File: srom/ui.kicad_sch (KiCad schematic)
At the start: 17 parts, among them J301 Conn_01x10_Female, J303 Conn_01x03_Female, SW301 SW_MEC_5E, SW302 RotaryEncoder_Switch, SW303 SW_MEC_5E, U301 Pico-3 UI

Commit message: first draft of daughterboard taking shape
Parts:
- removed D301, D302, D303, D304, D305, D306, D307, D308: LED_Small, LED_THT:LED_D3.0mm, symbol Device:LED_Small
- removed SW301, SW303: SW_MEC_5E, Button_Switch_THT:SW_PUSH_6mm_H4.3mm, symbol Switch:SW_MEC_5E
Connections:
- net 3V3_PICO3: now also J?.2 (Pin_2); no longer J?.5 (Pin_5)
- net ACTION_SW: now also J?.5 (Pin_5); no longer J?.2 (Pin_2)
- net CANCEL_SW: now also J?.6 (Pin_6); no longer J?.1 (Pin_1)
- net GND: now also J?.1 (Pin_1); no longer J?.6 (Pin_6)
- net OLED_SCK: now also J?.3 (Pin_3); no longer J?.4 (Pin_4)
- net OLED_SDA: now also J?.4 (Pin_4); no longer J?.3 (Pin_3)
- no-connect marks 16 -> 8
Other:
- note added: "Connection off to the 8 motor LEDs. The LEDs themselves are mounted on the daugherboard."
- note added: "I2C connection to OLED screen. Internal pullups work fine. SSH1106 based 1.3" screen is ideal, but C SDK doesn't seem to support it. Use SSH1306 0.96" screen for now, that's supported. The external user interface devices board connects here and on the connector for the LEDs. These provide a decent physical connection for the daughterboard."
- note removed: "I2C connection to OLED screen. Internal pullups work fine. SSH1106 based 1.3" screen is ideal, but C SDK doesn't seem to support it. Use SSH1306 0.96" screen for now, that's supported."
- note removed: "LED are excluded from the board. The signals from the GPIOs go to a header, LEDs connect to the header and are physically mounted on a panel."
- note removed: "LEDs for microdrive motor on. Use 3mm red one, like on the original drive. MOVE THESE TO EXTERNAL BOARD"
- note removed: "Two active-low switched inputs to the Pico UI. "Action" and "Cancel" UI functions. MOVE THESE TO EXTERNAL BOARD"
- moved on the sheet: J301, J?, R308

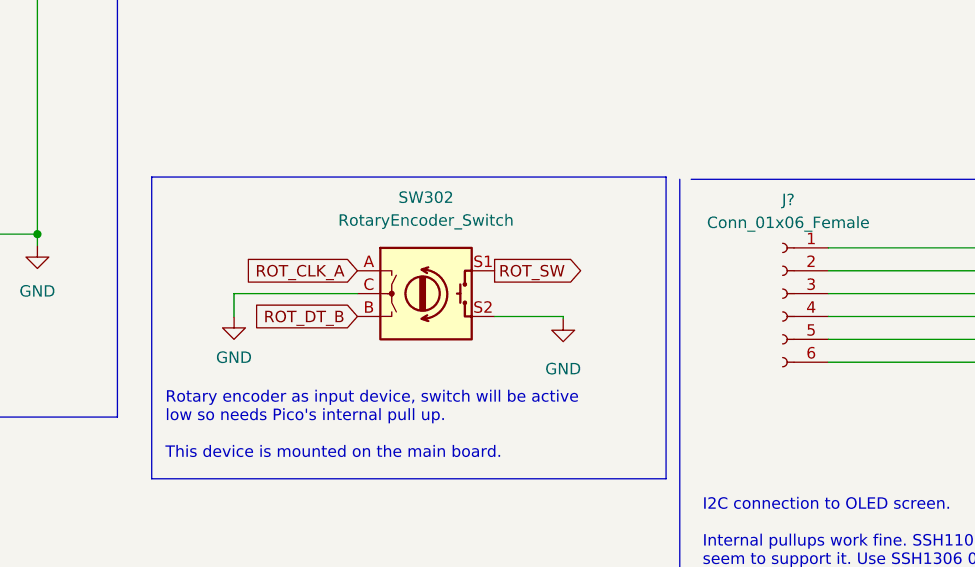
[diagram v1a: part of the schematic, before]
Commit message: board layout work, 4 layers
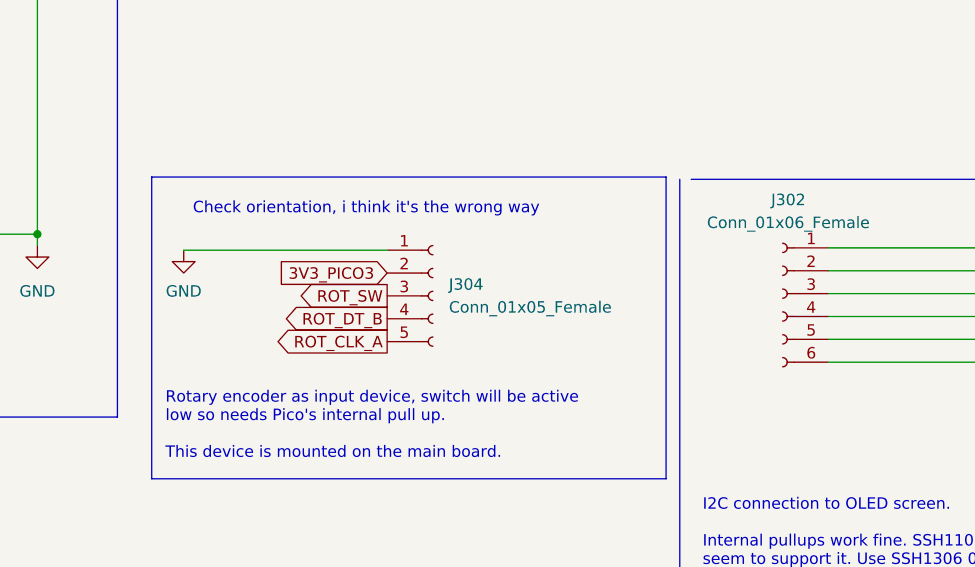
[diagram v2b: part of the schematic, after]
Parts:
- removed SW302: RotaryEncoder_Switch, Rotary_Encoder:RotaryEncoder_Bourns_Vertical_PEC12R-3xxxF-Sxxxx, symbol Device:RotaryEncoder_Switch
- added J304: Conn_01x05_Female, Connector_PinHeader_2.54mm:PinHeader_1x05_P2.54mm_Vertical, symbol Connector:Conn_01x05_Female
- J301: footprint (none) -> Connector_PinHeader_2.54mm:PinHeader_1x10_P2.54mm_Vertical
- J302: renamed from J?; footprint (none) -> Connector_PinHeader_2.54mm:PinHeader_1x06_P2.54mm_Vertical
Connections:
- net 3V3_PICO3: now also J304.2 (Pin_2)
- net GND: now also J304.1 (Pin_1)
- net ROT_CLK_A: now also J304.5 (Pin_5)
- net ROT_DT_B: now also J304.4 (Pin_4)
- net ROT_SW: now also J304.3 (Pin_3)
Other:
- note added: "Check orientation, i think it's the wrong way"
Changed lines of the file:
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@@
     (stroke (width 0) (type default) (color 0 0 0 0))
   )
-  (wire (pts (xy 141.224 118.364) (xy 141.224 120.904))
-    (stroke (width 0) (type default) (color 0 0 0 0))
-  )
-  (wire (pts (xy 141.224 118.364) (xy 154.94 118.364))
+  (wire (pts (xy 135.636 113.538) (xy 158.242 113.538))
     (stroke (width 0) (type default) (color 0 0 0 0))
   )
@@
     (stroke (width 0) (type default) (color 0 0 0 0))
   )
-  (wire (pts (xy 170.18 120.904) (xy 177.8 120.904))
-    (stroke (width 0) (type default) (color 0 0 0 0))
-  )
   (wire (pts (xy 60.96 167.132) (xy 59.182 167.132))
     (stroke (width 0) (type default) (color 0 0 0 0))
@@
   )
   (wire (pts (xy 90.17 40.64) (xy 119.38 40.64))
-    (stroke (width 0) (type default) (color 0 0 0 0))
-  )
-  (wire (pts (xy 177.8 120.904) (xy 177.8 121.158))
     (stroke (width 0) (type default) (color 0 0 0 0))
   )
@@
     (effects (font (size 1.27 1.27)) (justify left bottom))
   )
+  (text "Check orientation, i think it's the wrong way\n" (at 136.652 109.728 0)
+    (effects (font (size 1.27 1.27)) (justify left bottom))
+  )
   (text "GPIOs for the\nrotary encoder.\nDon't need SW." (at 26.924 60.96 0)
     (effects (font (size 1.27 1.27)) (justify left bottom))
@@
     )
   )
-  (global_label "ROT_CLK_A" (shape input) (at 154.94 115.824 180) (fields_autoplaced)
-    (effects (font (size 1.27 1.27)) (justify right))
-    (property "Intersheet References" "${INTERSHEET_REFS}" (id 0) (at 142.3669 115.7446 0)
+  (global_label "ROT_CLK_A" (shape output) (at 158.242 123.698 180) (fields_autoplaced)
+    (effects (font (size 1.27 1.27)) (justify right))
+    (property "Intersheet References" "${INTERSHEET_REFS}" (id 0) (at 145.6689 123.6186 0)
       (effects (font (size 1.27 1.27)) (justify right) hide)
     )
@@
     )
   )
+  (global_label "3V3_PICO3" (shape input) (at 158.242 116.078 180) (fields_autoplaced)
+    (effects (font (size 1.27 1.27)) (justify right))
+    (property "Intersheet References" "${INTERSHEET_REFS}" (id 0) (at 145.6689 115.9986 0)
+      (effects (font (size 1.27 1.27)) (justify right) hide)
+    )
+  )
   (global_label "OLED_SDA" (shape output) (at 54.61 50.8 180) (fields_autoplaced)
     (effects (font (size 1.27 1.27)) (justify right))
@@
     )
   )
-  (global_label "ROT_DT_B" (shape input) (at 154.94 120.904 180) (fields_autoplaced)
-    (effects (font (size 1.27 1.27)) (justify right))
-    (property "Intersheet References" "${INTERSHEET_REFS}" (id 0) (at 143.5159 120.8246 0)
+  (global_label "ROT_DT_B" (shape output) (at 158.242 121.158 180) (fields_autoplaced)
+    (effects (font (size 1.27 1.27)) (justify right))
+    (property "Intersheet References" "${INTERSHEET_REFS}" (id 0) (at 146.8179 121.2374 0)
       (effects (font (size 1.27 1.27)) (justify right) hide)
     )
@@
     )
   )
-  (global_label "ROT_SW" (shape output) (at 170.18 115.824 0) (fields_autoplaced)
-    (effects (font (size 1.27 1.27)) (justify left))
-    (property "Intersheet References" "${INTERSHEET_REFS}" (id 0) (at 179.7898 115.7446 0)
-      (effects (font (size 1.27 1.27)) (justify left) hide)
+  (global_label "ROT_SW" (shape output) (at 158.242 118.618 180) (fields_autoplaced)
+    (effects (font (size 1.27 1.27)) (justify right))
+    (property "Intersheet References" "${INTERSHEET_REFS}" (id 0) (at 148.6322 118.6974 0)
+      (effects (font (size 1.27 1.27)) (justify right) hide)
     )
   )
@@
       (effects (font (size 1.27 1.27)) (justify left))
     )
-    (property "Footprint" "" (id 2) (at 66.04 156.972 0)
+    (property "Footprint" "Connector_PinHeader_2.54mm:PinHeader_1x10_P2.54mm_Vertical" (id 2) (at 66.04 156.972 0)
       (effects (font (size 1.27 1.27)) hide)
     )
@@
   (symbol (lib_id "Connector:Conn_01x06_Female") (at 202.184 118.364 0) (mirror y) (unit 1)
     (in_bom yes) (on_board yes) (fields_autoplaced)
-    (property "Reference" "J?" (id 0) (at 202.819 107.95 0))
+    (property "Reference" "J302" (id 0) (at 202.819 107.95 0))
     (property "Value" "Conn_01x06_Female" (id 1) (at 202.819 110.49 0))
-    (property "Footprint" "" (id 2) (at 202.184 118.364 0)
+    (property "Footprint" "Connector_PinHeader_2.54mm:PinHeader_1x06_P2.54mm_Vertical" (id 2) (at 202.184 118.364 0)
       (effects (font (size 1.27 1.27)) hide)
     )
@@
     (pin "9")
   )
-  (symbol (lib_id "Device:RotaryEncoder_Switch") (at 162.56 118.364 0) (unit 1)
-    (in_bom yes) (on_board yes) (fields_autoplaced)
-    (property "Reference" "SW302" (id 0) (at 162.56 107.696 0))
-    (property "Value" "RotaryEncoder_Switch" (id 1) (at 162.56 110.236 0))
-    (property "Footprint" "Rotary_Encoder:RotaryEncoder_Bourns_Vertical_PEC12R-3xxxF-Sxxxx" (id 2) (at 158.75 114.3 0)
-      (effects (font (size 1.27 1.27)) hide)
-    )
-    (property "Datasheet" "~" (id 3) (at 162.56 111.76 0)
-      (effects (font (size 1.27 1.27)) hide)
-    )
-    (pin "A")
-    (pin "B")
-    (pin "C")
-    (pin "S1")
-    (pin "S2")
-  )
   (symbol (lib_id "power:GND") (at 119.38 113.03 0) (unit 1)
     (in_bom yes) (on_board yes) (fields_autoplaced)
@@
     (pin "1")
   )
-  (symbol (lib_id "power:GND") (at 141.224 120.904 0) (unit 1)
-    (in_bom yes) (on_board yes) (fields_autoplaced)
-    (property "Reference" "#PWR0302" (id 0) (at 141.224 127.254 0)
-      (effects (font (size 1.27 1.27)) hide)
-    )
-    (property "Value" "GND" (id 1) (at 141.224 125.476 0))
-    (property "Footprint" "" (id 2) (at 141.224 120.904 0)
-      (effects (font (size 1.27 1.27)) hide)
-    )
-    (property "Datasheet" "" (id 3) (at 141.224 120.904 0)
-      (effects (font (size 1.27 1.27)) hide)
-    )
-    (pin "1")
+  (symbol (lib_id "power:GND") (at 135.636 113.538 0) (unit 1)
+    (in_bom yes) (on_board yes) (fields_autoplaced)
+    (property "Reference" "#PWR0302" (id 0) (at 135.636 119.888 0)
+      (effects (font (size 1.27 1.27)) hide)
+    )
+    (property "Value" "GND" (id 1) (at 135.636 118.11 0))
+    (property "Footprint" "" (id 2) (at 135.636 113.538 0)
+      (effects (font (size 1.27 1.27)) hide)
+    )
+    (property "Datasheet" "" (id 3) (at 135.636 113.538 0)
+      (effects (font (size 1.27 1.27)) hide)
+    )
+    (pin "1")
+  )
+  (symbol (lib_id "Connector:Conn_01x05_Female") (at 163.322 118.618 0) (unit 1)
+    (in_bom yes) (on_board yes) (fields_autoplaced)
+    (property "Reference" "J304" (id 0) (at 165.1 117.3479 0)
+      (effects (font (size 1.27 1.27)) (justify left))
+    )
+    (property "Value" "Conn_01x05_Female" (id 1) (at 165.1 119.8879 0)
+      (effects (font (size 1.27 1.27)) (justify left))
+    )
+    (property "Footprint" "Connector_PinHeader_2.54mm:PinHeader_1x05_P2.54mm_Vertical" (id 2) (at 163.322 118.618 0)
+      (effects (font (size 1.27 1.27)) hide)
+    )
+    (property "Datasheet" "~" (id 3) (at 163.322 118.618 0)
+      (effects (font (size 1.27 1.27)) hide)
+    )
+    (pin "1")
+    (pin "2")
+    (pin "3")
+    (pin "4")
+    (pin "5")
   )
   (symbol (lib_id "pico-sym:Pico") (at 72.39 59.69 0) (unit 1)
@@
       (effects (font (size 1.27 1.27)) hide)
     )
-    (pin "1")
-  )
-  (symbol (lib_id "power:GND") (at 177.8 121.158 0) (unit 1)
-    (in_bom yes) (on_board yes) (fields_autoplaced)
-    (property "Reference" "#PWR0305" (id 0) (at 177.8 127.508 0)
-      (effects (font (size 1.27 1.27)) hide)
-    )
-    (property "Value" "GND" (id 1) (at 177.8 126.746 0))
-    (property "Footprint" "" (id 2) (at 177.8 121.158 0)
-      (effects (font (size 1.27 1.27)) hide)
-    )
-    (property "Datasheet" "" (id 3) (at 177.8 121.158 0)
-      (effects (font (size 1.27 1.27)) hide)
-    )

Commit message: more work on the new pcb, i think i have the basic layout now
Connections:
- net 3V3_PICO3: no longer J304.2 (Pin_2)
- new net 3V3_PICO1: J304.2 (Pin_2)
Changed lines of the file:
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@@
     )
   )
-  (global_label "3V3_PICO3" (shape input) (at 158.242 116.078 180) (fields_autoplaced)
+  (global_label "3V3_PICO1" (shape input) (at 158.242 116.078 180) (fields_autoplaced)
     (effects (font (size 1.27 1.27)) (justify right))
     (property "Intersheet References" "${INTERSHEET_REFS}" (id 0) (at 145.6689 115.9986 0)

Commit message: final pcb? about to copy layout for daughterboard
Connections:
- net OLED_SCK: now also U301.7 (GPIO5); no longer U301.6 (GPIO4)
- net OLED_SDA: now also U301.6 (GPIO4); no longer U301.7 (GPIO5)
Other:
- note removed: "Check orientation, i think it's the wrong way"
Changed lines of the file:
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@@
-    (effects (font (size 1.27 1.27)) (justify left bottom))
-  )
-  (text "Check orientation, i think it's the wrong way\n" (at 136.652 109.728 0)
     (effects (font (size 1.27 1.27)) (justify left bottom))
   )
@@
     )
   )
-  (global_label "OLED_SDA" (shape output) (at 54.61 50.8 180) (fields_autoplaced)
+  (global_label "OLED_SDA" (shape output) (at 54.61 48.26 180) (fields_autoplaced)
     (effects (font (size 1.27 1.27)) (justify right))
-    (property "Intersheet References" "${INTERSHEET_REFS}" (id 0) (at 42.8836 50.7206 0)
+    (property "Intersheet References" "${INTERSHEET_REFS}" (id 0) (at 42.8836 48.1806 0)
       (effects (font (size 1.27 1.27)) (justify right) hide)
     )
@@
     )
   )
-  (global_label "OLED_SCK" (shape output) (at 54.61 48.26 180) (fields_autoplaced)
+  (global_label "OLED_SCK" (shape output) (at 54.61 50.8 180) (fields_autoplaced)
     (effects (font (size 1.27 1.27)) (justify right))
-    (property "Intersheet References" "${INTERSHEET_REFS}" (id 0) (at 42.7021 48.1806 0)
+    (property "Intersheet References" "${INTERSHEET_REFS}" (id 0) (at 42.7021 50.7206 0)
       (effects (font (size 1.27 1.27)) (justify right) hide)
     )
